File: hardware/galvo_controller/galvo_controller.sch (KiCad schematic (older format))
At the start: 65 parts, among them J1 Conn_Coaxial, J2 Conn_Coaxial, J3 Conn_01x03, J4 Conn_01x03, U1 PCM3060, U2 OPA2134, U3 LME49724, U4 LME49724

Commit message: Working on schematic
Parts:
- removed C3, C4, C? (x9): 0.1u, symbol C
- removed C? (x9): 10u, symbol CP
- added C1, C10, C23, C24, C25, C26, C27, C31, C32, C33, C5, C7, C8: 10u, Capacitors_SMD:C_0805, symbol C
- added C13, C14, C21, C22, C28, C29, C30, C34, C35, C36, C9: 0.1u, Capacitors_SMD:C_0603, symbol C
- added C3, C4: 100u, symbol CP
- added R1, R2: 10k, Resistors_SMD:R_0603, symbol R
- added U1: Teensy3.6, symbol Teensy3.6
- added U2: L78L33, TO_SOT_Packages_SMD:SOT89-3_Housing, symbol L78L33_SOT89
- added U4: L78L05, TO_SOT_Packages_SMD:SOT89-3_Housing, symbol L78L05_SOT89
- C11: footprint (none) -> Capacitors_SMD:C_0805; Part (none) -> 490-5523-1-ND; Source (none) -> DigiKey
- C12: value 10u -> 0.1u; footprint (none) -> Capacitors_SMD:C_0603; Part (none) -> 490-9691-1-ND; Source (none) -> DigiKey
- C2: value 0.1u -> 10u; footprint (none) -> Capacitors_SMD:C_0805; Part (none) -> 490-5523-1-ND; Source (none) -> DigiKey
- C6: renamed from C?; footprint (none) -> Capacitors_SMD:C_0603; Part (none) -> 490-9691-1-ND; Source (none) -> DigiKey
- D1, D2, D3, D4: value D -> 1N4148W; Part (none) -> 1N4148W-FDICT-ND; Source (none) -> DigiKey
- J4: renamed from J1; value Conn_Coaxial -> Red; Part (none) -> CP-1401-ND; Source (none) -> DigiKey
- J5: renamed from J2; value Conn_Coaxial -> White; Part (none) -> CP-1402-ND; Source (none) -> DigiKey
- R10: renamed from R8; footprint (none) -> Resistors_SMD:R_0603
- R11: renamed from R9; footprint (none) -> Resistors_SMD:R_0603
- R12: renamed from R10; footprint (none) -> Resistors_SMD:R_0603
- R13: renamed from R11; footprint (none) -> Resistors_SMD:R_0603
- R14: renamed from R12; footprint (none) -> Resistors_SMD:R_0603
- R15: renamed from R13; footprint (none) -> Resistors_SMD:R_0603
- R16: renamed from R14; footprint (none) -> Resistors_SMD:R_0603
- R17: renamed from R15; footprint (none) -> Resistors_SMD:R_0603
- R18: renamed from R16; footprint (none) -> Resistors_SMD:R_0603
- R19: renamed from R17; footprint (none) -> Resistors_SMD:R_0603
- R20: renamed from R18; footprint (none) -> Resistors_SMD:R_0603
- R21: renamed from R19; footprint (none) -> Resistors_SMD:R_0603
- R22: renamed from R20; footprint (none) -> Resistors_SMD:R_0603
- R3: renamed from R1; footprint (none) -> Resistors_SMD:R_0603
- R4: renamed from R2; footprint (none) -> Resistors_SMD:R_0603
- R5: renamed from R3; footprint (none) -> Resistors_SMD:R_0603
- R6: renamed from R4; footprint (none) -> Resistors_SMD:R_0603
- R7: renamed from R5; footprint (none) -> Resistors_SMD:R_0603
- R8: renamed from R6; footprint (none) -> Resistors_SMD:R_0603
- R9: renamed from R7; footprint (none) -> Resistors_SMD:R_0603
- U3: renamed from U1; Part (none) -> 296-38201-1-ND; Source (none) -> DigiKey
- U5: renamed from U2; Part (none) -> 296-22024-1-ND; Source (none) -> DigiKey
- U6: renamed from U3; Part (none) -> 296-37390-1-ND; Source (none) -> DigiKey
- U7: renamed from U4; Part (none) -> 296-37390-1-ND; Source (none) -> DigiKey
- gave numbers to parts that had none: 3
- renumbered C5 to C15, C6 to C16, C7 to C17, C8 to C18, C9 to C19, C10 to C20, J3 to J6, J4 to J7
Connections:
- net labels added: RX, TX
- net labels removed: DIN, DOUT, RST
- wire segments 230 -> 270
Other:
- moved on the sheet: C6, J1, J2, J3

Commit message: Working on schematic
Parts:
- removed D1, D2, D3, D4: 1N4148W, symbol D
- added C1, C3: 10u, Capacitors_SMD:C_0805, symbol C
- added D1, D2: BAT54S, TO_SOT_Packages_SMD:SOT-23, symbol D_Schottky_x2_Serial_AKC
- added J1: Conn_01x03, Connectors_JST:JST_XH_B03B-XH-A_03x2.50mm_Straight, symbol Conn_01x03
- added Q1: DDTD113ZC, TO_SOT_Packages_SMD:SOT-23, symbol Q_NPN_BEC
- added R1: 2.2k, Resistors_SMD:R_0603, symbol R
- added U1: L78L05, TO_SOT_Packages_SMD:SOT89-3_Housing, symbol L78L05_SOT89
- C17: renamed from C15; value C -> 330p
- C18: renamed from C16; value C -> 330p
- C5: renamed from C3; footprint (none) -> Capacitors_SMD:CP_Elec_6.3x7.7
- C6: renamed from C4; footprint (none) -> Capacitors_SMD:CP_Elec_6.3x7.7
- J2: renamed from J1; footprint (none) -> Connectors_JST:JST_XH_B03B-XH-A_03x2.50mm_Straight; Part (none) -> 455-2248-ND; Source (none) -> DigiKey
- J3: renamed from J2; footprint (none) -> Connectors_JST:JST_XH_B03B-XH-A_03x2.50mm_Straight; Part (none) -> 455-2248-ND; Source (none) -> DigiKey
- J4: renamed from J3; footprint (none) -> Connectors_JST:JST_XH_B03B-XH-A_03x2.50mm_Straight; Part (none) -> 455-2248-ND; Source (none) -> DigiKey
- J7: renamed from J6; footprint (none) -> Connectors_JST:JST_XH_B03B-XH-A_03x2.50mm_Straight; Part (none) -> 455-2248-ND; Source (none) -> DigiKey
- J8: renamed from J7; footprint (none) -> Connectors_JST:JST_XH_B03B-XH-A_03x2.50mm_Straight; Part (none) -> 455-2248-ND; Source (none) -> DigiKey
- R12: renamed from R11; value R -> 10k
- R13: renamed from R12; value R -> 10k
- R18: renamed from R17; value R -> 0
- R19: renamed from R18; value R -> 0
- R6: renamed from R5; value R -> 8.06k
- R7: renamed from R6; value R -> 8.06k
- U4: renamed from U3; footprint (none) -> Housings_SSOP:TSSOP-28_4.4x9.7mm_Pitch0.65mm
- U6: renamed from U5; footprint (none) -> Housings_SOIC:SOIC-8_3.9x4.9mm_Pitch1.27mm
- U7: renamed from U6; footprint Housings_DFN_QFN:DFN-8-1EP_3x3mm_Pitch0.5mm -> Housings_SOIC:SOIC-8-1EP_3.9x4.9mm_Pitch1.27mm
- U8: renamed from U7; footprint Housings_DFN_QFN:DFN-8-1EP_3x3mm_Pitch0.5mm -> Housings_SOIC:SOIC-8-1EP_3.9x4.9mm_Pitch1.27mm
- renumbered C8 to C10, C9 to C11, C10 to C12, C11 to C13, C12 to C14, C13 to C15, C14 to C16, C17 to C19, C1 to C2, C18 to C20, C19 to C21, C20 to C22, C21 to C23, C22 to C24, C23 to C25, C24 to C26, C25 to C27, C26 to C28, C27 to C29, C28 to C30, C29 to C31, C30 to C32, C31 to C33, C32 to C34, C33 to C35, C34 to C36, C35 to C37, C36 to C38, C2 to C4, C5 to C7, C6 to C8, C7 to C9, J4 to J5, J5 to J6, R9 to R10, R10 to R11, R13 to R14, R14 to R15, R15 to R16, R16 to R17, R1 to R2, R19 to R20, R20 to R21, R21 to R22, R22 to R23, R2 to R3, R3 to R4, R4 to R5, R7 to R8, R8 to R9, U1 to U2, U2 to U3, U4 to U5
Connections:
- net labels added: LASER_EN
- wire segments 270 -> 291
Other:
- moved on the sheet: R2, R3

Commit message: Switched to ESP32 microcontroller
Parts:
- removed U2: Teensy3.6, symbol Teensy3.6
- added C?: 10u, Capacitors_SMD:C_0805, symbol C
- added C?: 4.7u, symbol C
- added C?: C, symbol C
- added D?: RED, symbol LED
- added D?: GRN, symbol LED
- added J?: USB_OTG, symbol USB_OTG
- added Q? (x2): MMBT2222, symbol Q_NPN_BEC
- added R? (x2): R, symbol R
- added R? (x3): 10k, Resistors_SMD:R_0603, symbol R
- added U?: ESP-WROOM-32D, symbol ESP-WROOM-32D
- added U?: CP2104, symbol CP2104
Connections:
- net labels added: DTR, GPIO0, RESET, RTS, RXD0, TXD0
- wire segments 291 -> 337
- no-connect marks 2 -> 4
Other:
- note added: "TODO: CHECK IF REG CAN SUPPLY ENOUGH CURRENT FOR ESP32"
- moved on the sheet: C1, C12, C2, C3, C4, C5, C6, C9, J1, J2, J3, J4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

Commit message: Using switching regulator for 3.3V and 5V rails
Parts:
- removed C1, C2, C3: 10u, Capacitors_SMD:C_0805, symbol C
- removed U1: L78L05, TO_SOT_Packages_SMD:SOT89-3_Housing, symbol L78L05_SOT89
- removed U3: L78L33, TO_SOT_Packages_SMD:SOT89-3_Housing, symbol L78L33_SOT89
- added C10, C7: C, symbol C
- added C11: 1u, symbol C
- added C12, C6: 10u, Capacitors_SMD:C_0805, symbol C
- added C13, C5, C8, C9: 0.1u, Capacitors_SMD:C_0603, symbol C
- added C14: 22u, symbol C
- added J?: Micro_SD_Card, symbol Micro_SD_Card
- added L1: 2.2uH, symbol L
- added L2: 3.3uH, symbol L
- added R11: 124k, Resistors_SMD:R_0603, symbol R
- added R12, R4: 22.1k, Resistors_SMD:R_0603, symbol R
- added R3: 73.2k, Resistors_SMD:R_0603, symbol R
- added U3: TPS54295PWP, Housings_SSOP:HTSSOP-16-1EP_4.4x5mm_Pitch0.65mm_ThermalVias, symbol TPS54295PWP
- C4: value 10u -> 22u; footprint Capacitors_SMD:C_0805 -> (none); Part 490-5523-1-ND -> (none); Source DigiKey -> (none)
- R5, R7: renamed from R?; footprint (none) -> Resistors_SMD:R_0603
- U1: renamed from U?; footprint (none) -> footprint:ESP32-WROOM; Source (none) -> eBay
- U2: renamed from U?; footprint (none) -> Housings_DFN_QFN:QFN-24-1EP_4x4mm_Pitch0.5mm; Part (none) -> 336-2008-5-ND; Source (none) -> DigiKey
- gave numbers to parts that had none: 11
- renumbered C7 to C15, C8 to C16, C10 to C17, C9 to C18, C11 to C19, C5 to C20, C6 to C21, C12 to C22, C13 to C23, C14 to C24, C15 to C25, C16 to C26, C17 to C27, C18 to C28, C19 to C29, C20 to C30, C21 to C31, C22 to C32, C23 to C33, C24 to C34, C25 to C35, C26 to C36, C27 to C37, C28 to C38, C29 to C39, C30 to C40, C31 to C41, C32 to C42, C33 to C43, C34 to C44, C35 to C45, C36 to C46, C37 to C47, C38 to C48, D1 to D3, D2 to D4, J1 to J2, J2 to J3, J3 to J4, J4 to J5, J5 to J6, J6 to J7, J7 to J8, J8 to J9, R4 to R13, R5 to R14, R6 to R15, R7 to R16, R8 to R17, R9 to R18, R10 to R19, R1 to R2, R11 to R20, R12 to R21, R13 to R22, R14 to R23, R15 to R24, R16 to R25, R17 to R26, R18 to R27, R19 to R28, R20 to R29, R21 to R30, R22 to R31, R23 to R32, R2 to R6, R3 to R8
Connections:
- net labels added: +5VA, +5VD
- net labels removed: +5V
- wire segments 337 -> 364
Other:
- note removed: "TODO: CHECK IF REG CAN SUPPLY ENOUGH CURRENT FOR ESP32"
- moved on the sheet: C1, C18, C2, C20, C21, C22, C3, D1, D2, J1, J2, Q1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

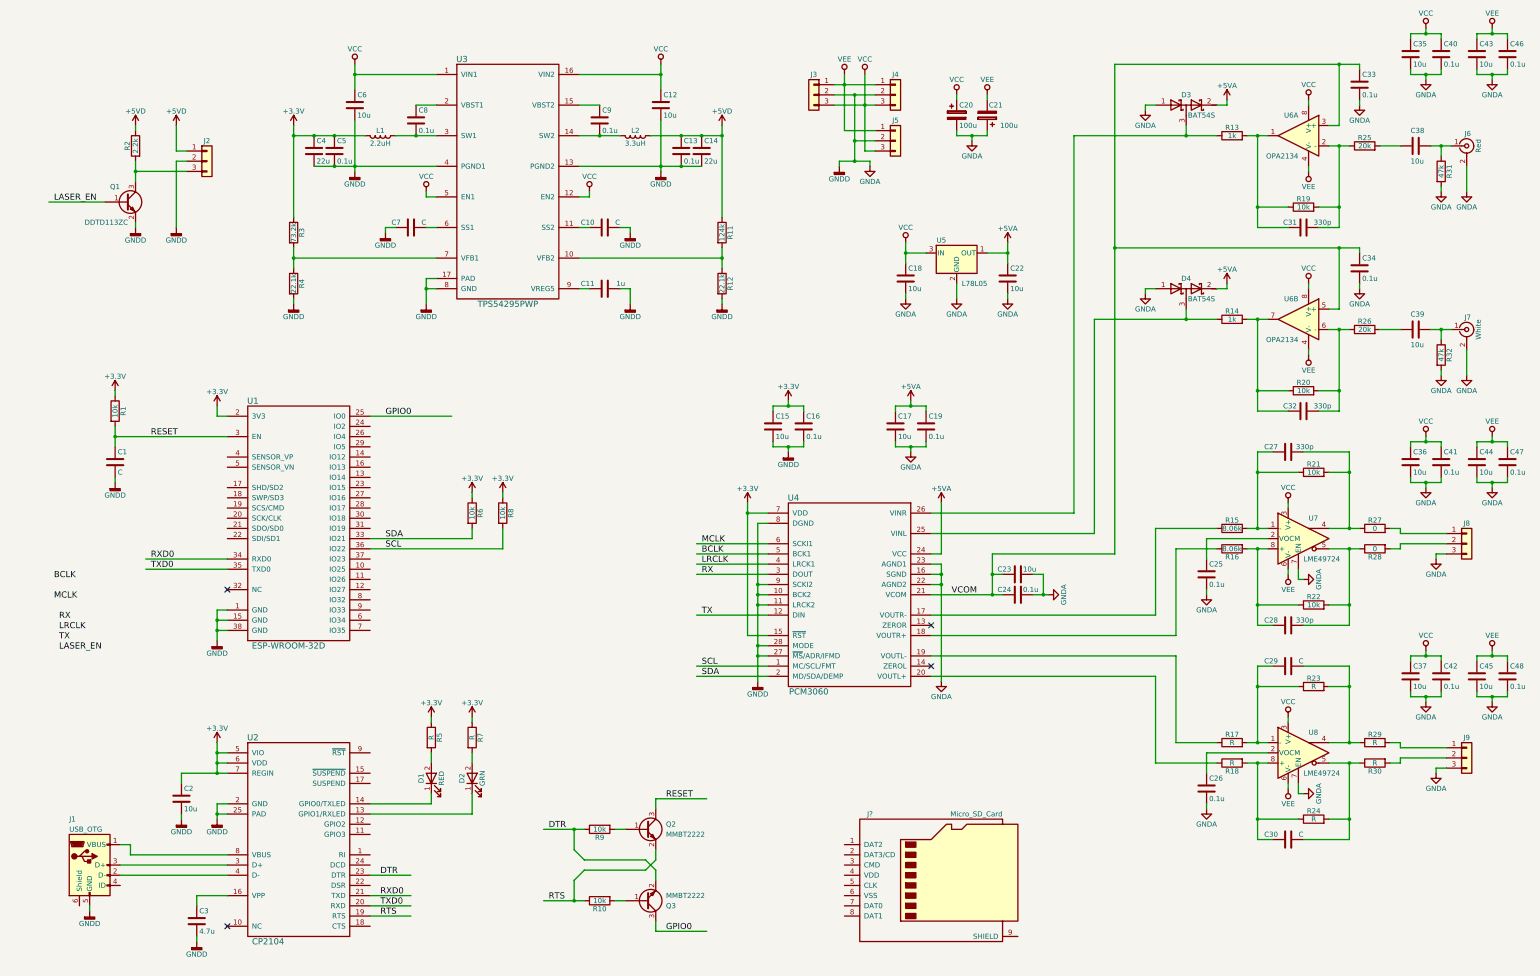
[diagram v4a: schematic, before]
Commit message: Changed to single buck DC DC converter
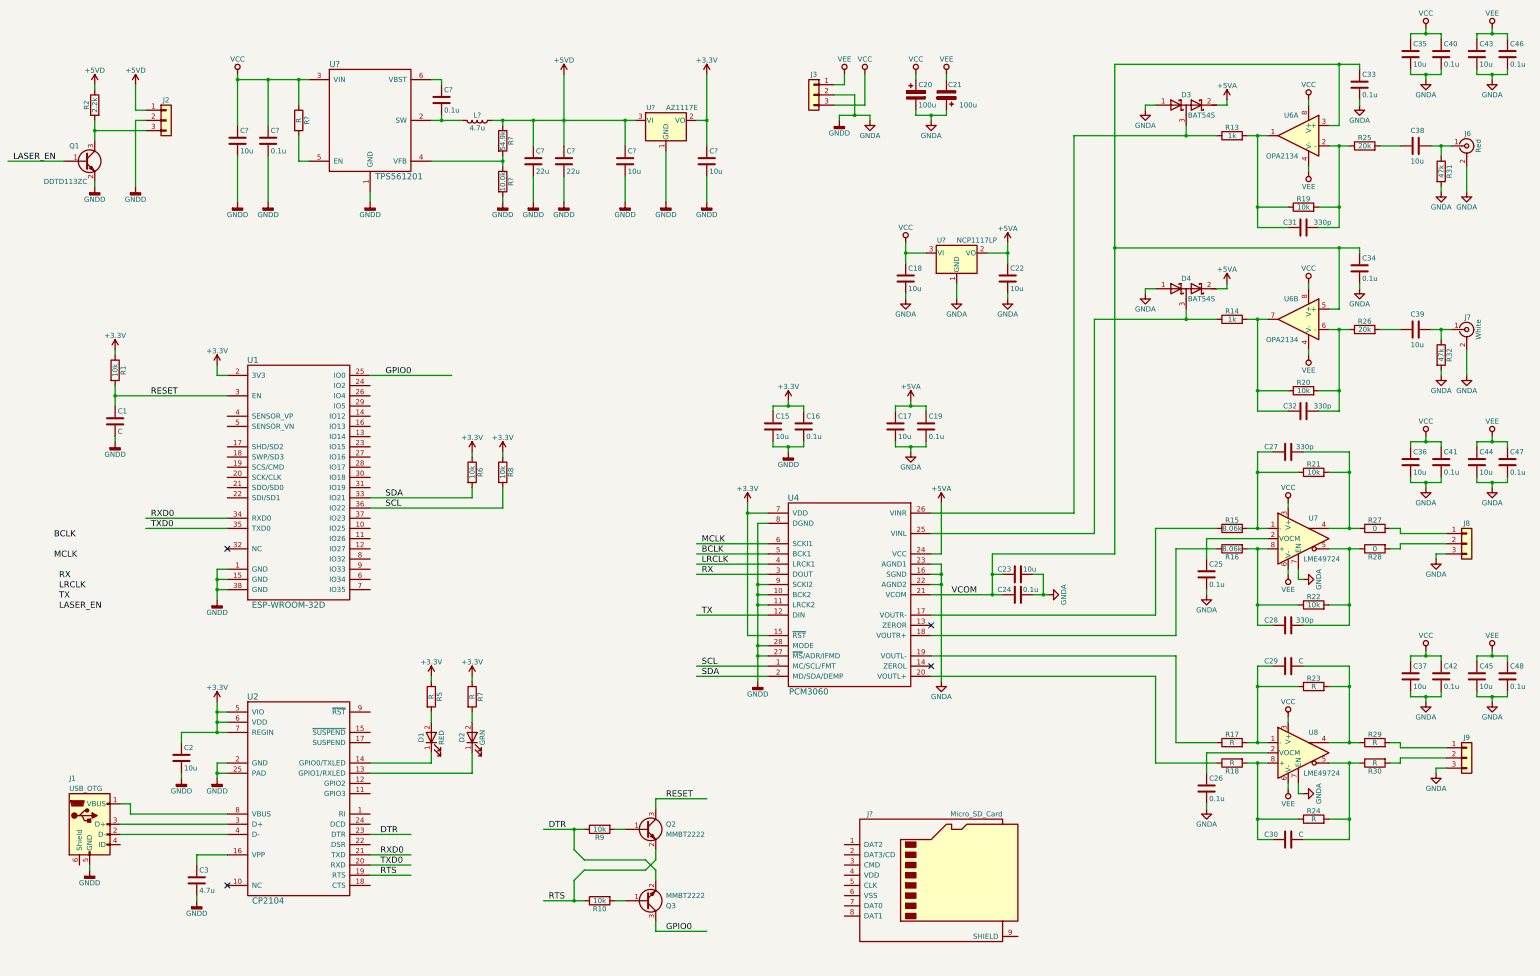
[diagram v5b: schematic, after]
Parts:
- removed C10, C7: C, symbol C
- removed C11: 1u, symbol C
- removed C12, C6: 10u, Capacitors_SMD:C_0805, symbol C
- removed C13, C5, C8, C9: 0.1u, Capacitors_SMD:C_0603, symbol C
- removed C14, C4: 22u, symbol C
- removed J4, J5: Conn_01x03, Connectors_JST:JST_XH_B03B-XH-A_03x2.50mm_Straight, symbol Conn_01x03
- removed L1: 2.2uH, symbol L
- removed L2: 3.3uH, symbol L
- removed R11: 124k, Resistors_SMD:R_0603, symbol R
- removed R12, R4: 22.1k, Resistors_SMD:R_0603, symbol R
- removed R3: 73.2k, Resistors_SMD:R_0603, symbol R
- removed U3: TPS54295PWP, Housings_SSOP:HTSSOP-16-1EP_4.4x5mm_Pitch0.65mm_ThermalVias, symbol TPS54295PWP
- removed U5: L78L05, TO_SOT_Packages_SMD:SOT89-3_Housing, symbol L78L05_SOT89
- added C? (x2): 0.1u, Capacitors_SMD:C_0603, symbol C
- added C? (x3): 10u, Capacitors_SMD:C_0805, symbol C
- added C? (x2): 22u, symbol C
- added L?: 4.7u, symbol L
- added R?: 54.9k, symbol R
- added R?: 10.0k, symbol R
- added R?: R, symbol R
- added U?: TPS561201, symbol TPS561201
- added U?: AZ1117E, TO_SOT_Packages_SMD:SOT-223, symbol AZ1117-3.3
- added U?: NCP1117LP, TO_SOT_Packages_SMD:SOT-223, symbol NCP1117-5.0_SOT223
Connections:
- wire segments 364 -> 351
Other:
- moved on the sheet: C1, C2, C20, C21, C3, D1, D2, J1, J2, Q1, R1, R2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

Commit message: Working on schematic
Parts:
- added D3: ORG, Diodes_SMD:D_0603, symbol LED
- added R10: 1k, Resistors_SMD:R_0603, symbol R
- C1: value C -> 0.1u; footprint (none) -> Capacitors_SMD:C_0603; Part (none) -> 490-9691-1-ND; Source (none) -> DigiKey
- D1: footprint (none) -> Diodes_SMD:D_0603; Part (none) -> 160-1447-1-ND; Source (none) -> DigiKey
- D2: footprint (none) -> Diodes_SMD:D_0603; Part (none) -> 160-1435-1-ND; Source (none) -> DigiKey
- J1: footprint (none) -> footprint:10118192; Part (none) -> 609-4613-1-ND; Source (none) -> DigiKey
- L1: renamed from L?; Part (none) -> 732-1153-1-ND; Source (none) -> DigiKey
- R4: renamed from R5; value R -> 1k
- R6: renamed from R7; value R -> 1k
- gave numbers to parts that had none: 14
- renumbered C15 to C11, C16 to C12, C17 to C13, C18 to C14, C20 to C15, C19 to C16, C21 to C17, C22 to C18, C23 to C19, C24 to C20, C25 to C21, C26 to C22, C27 to C23, C28 to C24, C29 to C25, C30 to C26, C31 to C27, C32 to C28, C33 to C29, C34 to C30, C35 to C31, C36 to C32, C37 to C33, C38 to C34, C39 to C35, C40 to C36, C41 to C37, C42 to C38, C43 to C39, C44 to C40, C45 to C41, C46 to C42, C47 to C43, C48 to C44, D3 to D4, D4 to D5, J6 to J5, J7 to J6, J8 to J7, J9 to J8, R2 to R1, R9 to R11, R10 to R12, R1 to R2, R6 to R5, R8 to R9, U4 to U5, U6 to U7, U7 to U8, U8 to U9
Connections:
- net labels added: LED
- wire segments 351 -> 355
- no-connect marks 4 -> 8
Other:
- note added: "STRAPPING PINS\nIO0\nIO2\nIO5\nIO12\nIO15"

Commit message: Working on schematic
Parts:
- removed C6: 0.1u, Capacitors_SMD:C_0603, symbol C
- removed R7: 54.9k, symbol R
- removed R8: 10.0k, symbol R
- removed U3: TPS561201, symbol TPS561201
- removed U4: AZ1117E, TO_SOT_Packages_SMD:SOT-223, symbol AZ1117-3.3
- added C11: 10n, symbol C
- added C12: 1u, symbol C
- added C13: 10u, Capacitors_SMD:C_0805, symbol C
- added C15, C16: 22u, Capacitors_SMD:C_1206, symbol C
- added L2: 2.2u, symbol L
- added R12: 73.2k, Resistors_SMD:R_0603, symbol R
- added R13, R4: 22.1k, Resistors_SMD:R_0603, symbol R
- added U3: TPS54295PWP, Housings_SSOP:HTSSOP-16-1EP_4.4x5mm_Pitch0.65mm_ThermalVias, symbol TPS54295PWP
- C10, C9: value 10u -> 0.1u; footprint Capacitors_SMD:C_0805 -> Capacitors_SMD:C_0603; Part 490-5523-1-ND -> 490-9691-1-ND
- C4: value 10u -> 22u; footprint Capacitors_SMD:C_0805 -> Capacitors_SMD:C_1206; Part 490-5523-1-ND -> 311-1995-1-ND
- C5: value 0.1u -> 22u; footprint Capacitors_SMD:C_0603 -> Capacitors_SMD:C_1206; Part 490-9691-1-ND -> 311-1995-1-ND
- C7: value 22u -> 10u; footprint (none) -> Capacitors_SMD:C_0805; Part (none) -> 490-5523-1-ND; Source (none) -> DigiKey
- C8: value 22u -> 10n
- L1: value 4.7u -> 3.3u; Part 732-1153-1-ND -> 445-9554-1-ND
- R3: value R -> 124k; footprint (none) -> Resistors_SMD:R_0603
- renumbered C11 to C17, C12 to C18, C13 to C19, C14 to C20, C15 to C21, C16 to C22, C17 to C23, C18 to C24, C19 to C25, C20 to C26, C21 to C27, C22 to C28, C23 to C29, C24 to C30, C25 to C31, C26 to C32, C27 to C33, C28 to C34, C29 to C35, C30 to C36, C31 to C37, C32 to C38, C33 to C39, C34 to C40, C35 to C41, C36 to C42, C37 to C43, C38 to C44, C39 to C45, C40 to C46, C41 to C47, C42 to C48, C43 to C49, C44 to C50, R11 to R10, R12 to R11, R13 to R14, R14 to R15, R15 to R16, R16 to R17, R17 to R18, R18 to R19, R19 to R20, R20 to R21, R21 to R22, R22 to R23, R23 to R24, R24 to R25, R25 to R26, R26 to R27, R27 to R28, R28 to R29, R29 to R30, R30 to R31, R31 to R32, R32 to R33, R4 to R5, R5 to R6, R6 to R7, R9 to R8, R10 to R9, U5 to U4, U6 to U5, U7 to U6, U8 to U7, U9 to U8
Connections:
- wire segments 355 -> 365

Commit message: Working on schematic
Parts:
- added C25: 10u, Capacitors_SMD:C_0805, symbol C
- added JP1, JP2: Jumper_NO_Small, Pin_Headers:Pin_Header_Straight_1x02_Pitch2.54mm, symbol Jumper_NO_Small
- added R14, R15, R16, R17, R18, R19: 10k, Resistors_SMD:R_0603, symbol R
- C30: renamed from C31; value C -> 330p
- C31: renamed from C32; value C -> 330p
- R24: renamed from R18; value R -> 8.06k
- R25: renamed from R19; value R -> 8.06k
- R30: renamed from R24; value R -> 10k
- R31: renamed from R25; value R -> 10k
- R36: renamed from R30; value R -> 0
- R37: renamed from R31; value R -> 0
- renumbered C11 to C10, C12 to C11, C13 to C12, C15 to C13, C16 to C14, C17 to C15, C18 to C16, C19 to C17, C20 to C18, C21 to C19, C22 to C20, C23 to C21, C24 to C22, C25 to C23, C26 to C24, C27 to C26, C28 to C27, C29 to C28, C30 to C29, C33 to C32, C34 to C33, C35 to C34, C36 to C35, C37 to C36, C38 to C37, C39 to C38, C40 to C39, C41 to C40, C42 to C41, C43 to C42, C44 to C43, C45 to C44, C46 to C45, C47 to C46, C48 to C47, C49 to C48, C50 to C49, C7 to C6, C8 to C7, C9 to C8, C10 to C9, R11 to R10, R9 to R11, R14 to R20, R15 to R21, R16 to R22, R17 to R23, R20 to R26, R21 to R27, R22 to R28, R23 to R29, R26 to R32, R27 to R33, R28 to R34, R29 to R35, R32 to R38, R33 to R39, R10 to R9
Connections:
- net labels added: I2S_BCLK, I2S_LRCLK, I2S_MCLK, I2S_RX, I2S_TX, SD_CLK, SD_CMD, SD_DAT0, SD_DAT1, SD_DAT2, SD_DAT3
- net labels removed: BCLK, LRCLK, MCLK, RX, TX
- wire segments 365 -> 399
- no-connect marks 8 -> 5
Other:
- note added: "Bootstrap notes with SD card:\nIO2 - Needs to be driven low to enter serial program mode\nIO12 - Needs to be driven low to set flash prog voltage to 3.3V"
- moved on the sheet: C1, C2, C3, D1, D2, D3, J1, J4, Q2, Q3, R10, R11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
